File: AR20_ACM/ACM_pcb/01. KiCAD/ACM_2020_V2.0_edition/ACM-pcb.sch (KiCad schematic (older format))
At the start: 32 parts, among them J1 TC2030-MCP-NL, P1 Conn_02x15_Odd_Even, Q1 Q_PMOS_DMP3099L-13, U1 ATmega328P-AU, U2 MCP2542FDxMF, U3 NCV890430MW50TXG, U4 MCP2517FD-xSL, Y1 16.0Mhz

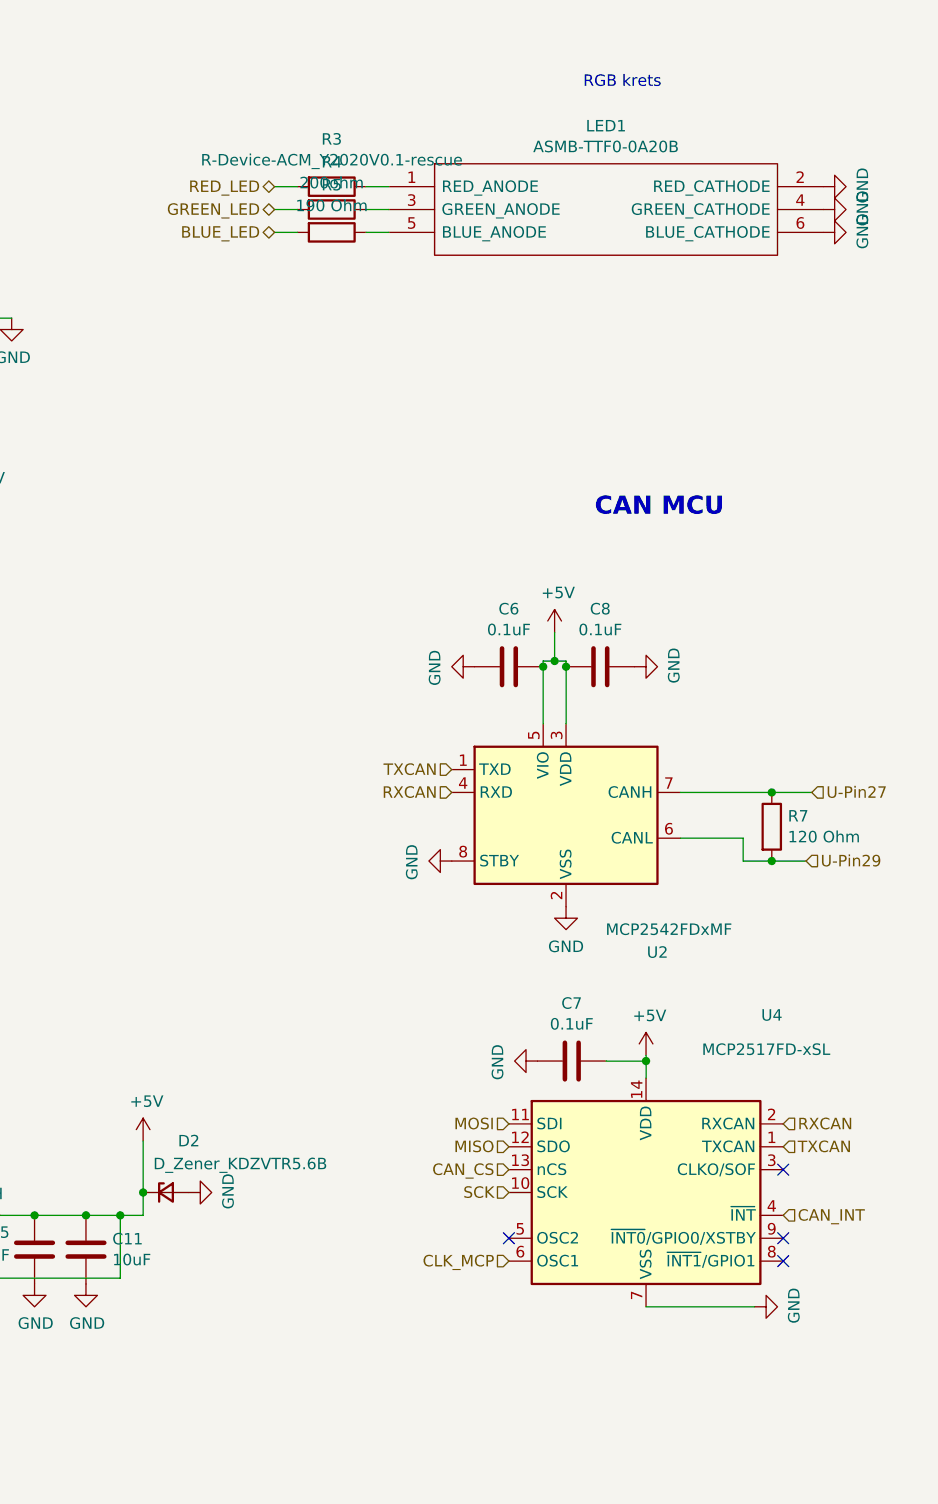
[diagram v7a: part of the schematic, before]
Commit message: 20Mhz resonator on CAN Conrtoller
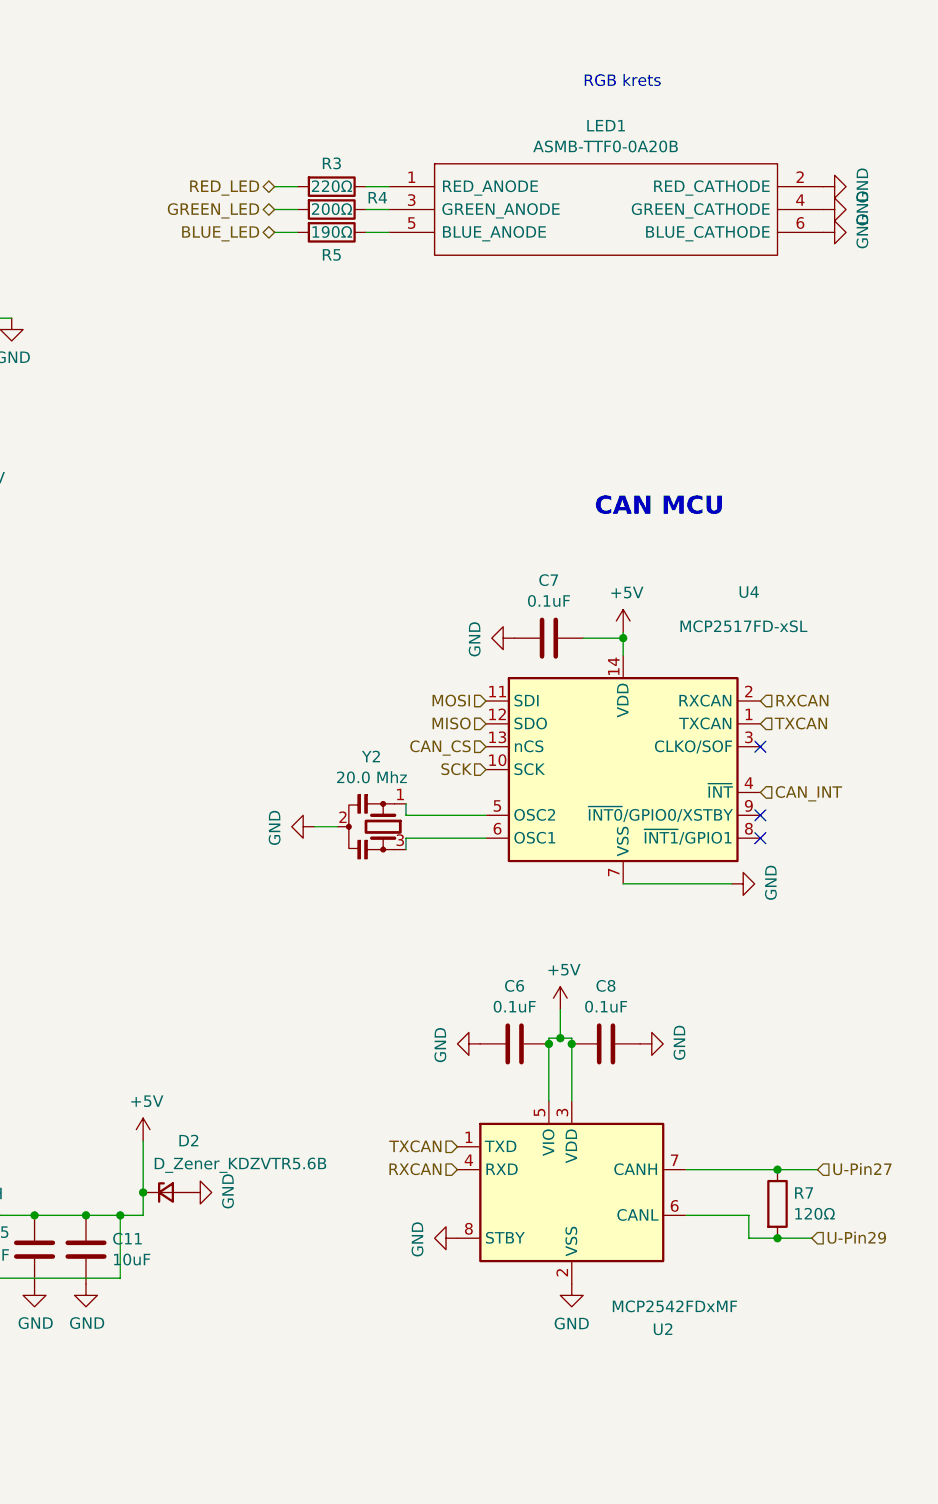
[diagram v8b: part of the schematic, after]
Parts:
- added Y2: 20.0 Mhz, ACM_2020_V2:Resonator_CSTNE20M0V51Z000R0, symbol ACM-pcb-rescue:Resonator_20Mhz_CSTNE20M0V51Z000R0
- R3: value R-Device-ACM_Y2020V0.1-rescue -> 220Ω
- R4: value 200ohm -> 200Ω
- R5: value 190 Ohm -> 190Ω
- R7: value 120 Ohm -> 120Ω
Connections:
- net CLK_MCP: no longer U4.6 (OSC1)
- net GND: now also Y2.2 (GND)
- net at U4.5 (OSC2): now also Y2.1 (Input)
- new net: U4.6 (OSC1), Y2.3 (Output)
- no-connect marks 4 -> 3
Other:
- moved on the sheet: C6, C7, C8, R7, U2, U4
